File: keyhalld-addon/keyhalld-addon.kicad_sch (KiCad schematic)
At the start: 66 parts, among them J1 Conn_01x06_Pin, J2 USB_C_Receptacle_USB2.0_16P, J3 Conn_01x04_Pin, SW1 SW_Push, SW10 RST, SW2 SW_Push, SW3 SW_Push, SW4 SW_Push, SW5 SW_Push, SW6 SW_Push, SW7 SW_Push, SW8 SW_Push, SW9 BOOT, U1 TLV1117-33, U2 RP2350A, U3 USBLC6-2SC6, U4 ER_OLEDM0.91_1x-I2C, Y1 12MHz

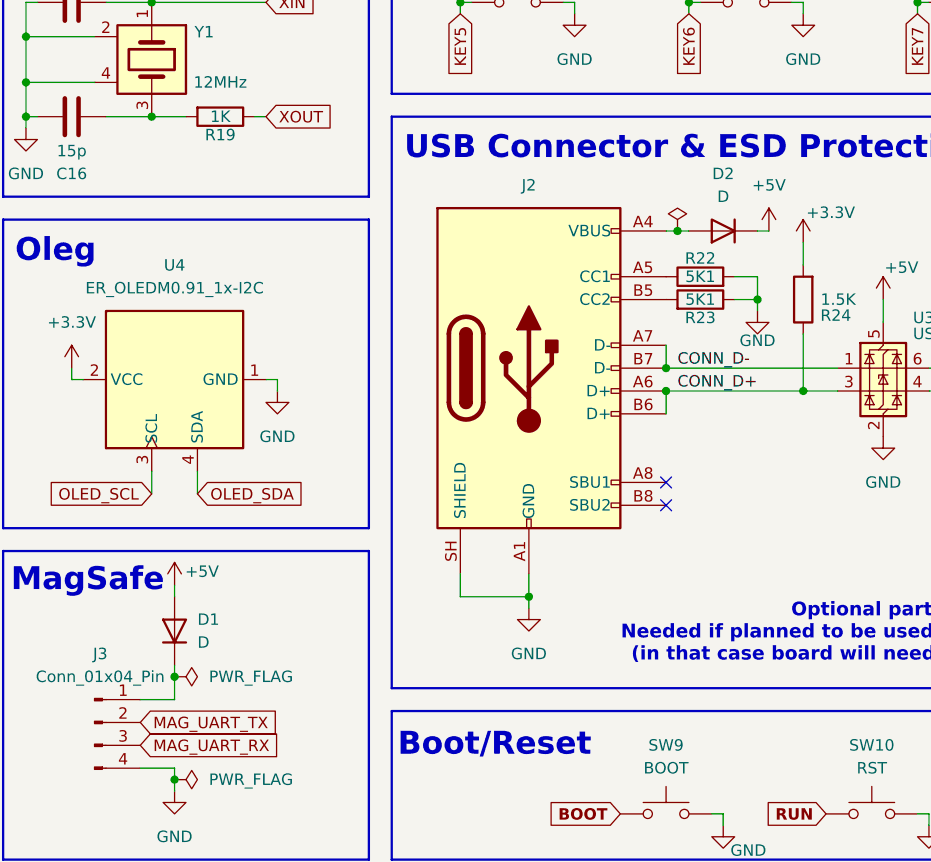
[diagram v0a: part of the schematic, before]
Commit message: fix diodes
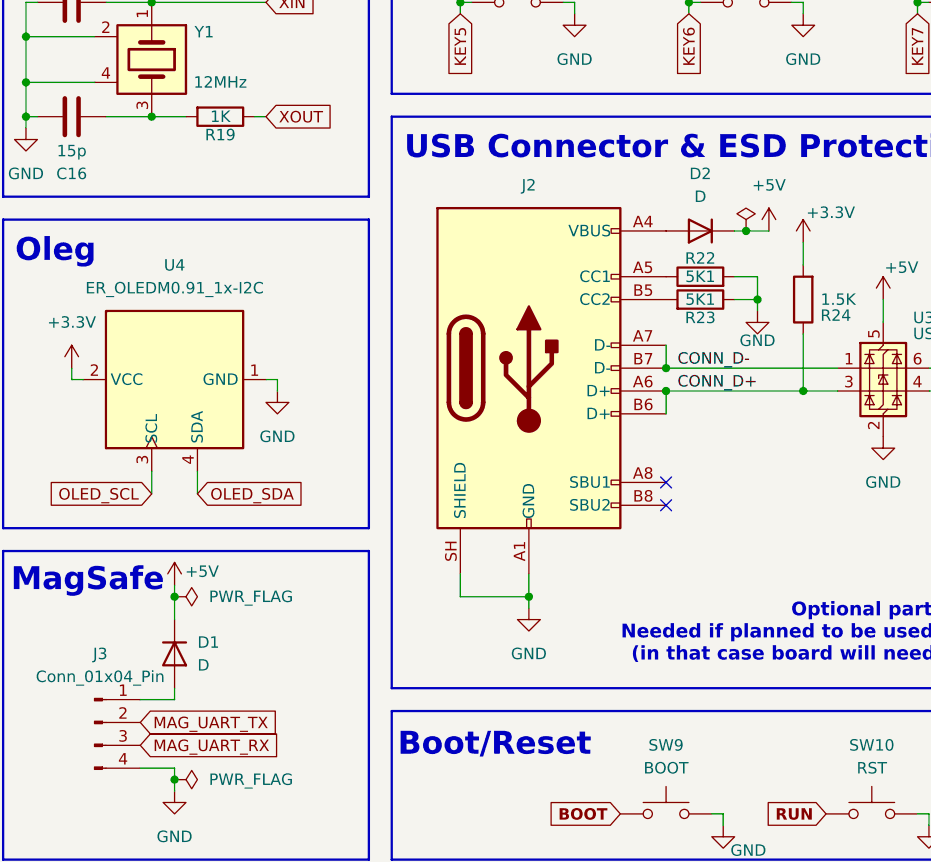
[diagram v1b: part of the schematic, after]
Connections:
- net +5V: now also D1.1 (K); no longer D1.2 (A)
- net at J3.1 (Pin_1): now also D1.2 (A); no longer D1.1 (K)

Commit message: add ws leds
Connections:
- net WS_LED: now reaches U2.41 (GPIO27_ADC1)
- no-connect marks 16 -> 15
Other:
- added sheet ws leds (ws_leds.kicad_sch)
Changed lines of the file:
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@@
 	)
 	(no_connect
-		(at 252.73 111.76)
-	)
-	(no_connect
 		(at 207.01 87.63)
 	)
@@
 		)
 	)
+	(global_label "WS_LED"
+		(shape input)
+		(at 252.73 111.76 0)
+		(fields_autoplaced yes)
+		(effects
+			(font
+				(size 1.27 1.27)
+			)
+			(justify left)
+		)
+		(property "Intersheetrefs" "${INTERSHEET_REFS}"
+			(at 262.7908 111.76 0)
+			(hide yes)
+			(show_name no)
+			(do_not_autoplace no)
+			(effects
+				(font
+					(size 1.27 1.27)
+				)
+				(justify left)
+			)
+		)
+	)
 	(global_label "EN_S_A"
 		(shape input)
@@
 				)
 			)
+		)
+	)
+	(sheet
+		(at 138.43 140.97)
+		(size 35.56 35.56)
+		(exclude_from_sim no)
+		(in_bom yes)
+		(on_board yes)
+		(dnp no)
+		(fields_autoplaced yes)
+		(stroke
+			(width 0.1524)
+			(type solid)
+		)
+		(fill
+			(color 204 204 255 1)
+		)
+		(property "Sheetname" "ws leds"
+			(at 138.43 140.2584 0)
+			(show_name no)
+			(do_not_autoplace no)
+			(effects
+				(font
+					(size 1.27 1.27)
+				)
+				(justify left bottom)
+			)
+		)
+		(property "Sheetfile" "ws_leds.kicad_sch"
+			(at 138.43 177.1146 0)
+			(show_name no)
+			(do_not_autoplace no)
+			(effects
+				(font
+					(size 1.27 1.27)
+				)
+				(justify left top)
+			)
+		)
+		(instances
+			(project "keyhalld-addon"
+				(path "/a8efb6d5-6c80-4ac0-bb97-11d91837bb7f"
+					(page "2")
+				)
+			)

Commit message: Super changes; FInal!
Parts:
- J3: footprint Connector_Wire:SolderWire-0.127sqmm_1x04_P3.7mm_D0.48mm_OD1mm -> Connector_PinHeader_2.54mm:PinHeader_1x04_P2.54mm_Vertical
- renumbered D2 to D1, D1 to D2
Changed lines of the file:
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@@
 		(dnp no)
 		(fields_autoplaced yes)
-		(property "Reference" "D2"
+		(property "Reference" "D1"
 			(at 91.44 119.38 0)
 			(show_name no)
@@
 			(project "keyhalld-addon"
 				(path "/a8efb6d5-6c80-4ac0-bb97-11d91837bb7f"
-					(reference "D2")
+					(reference "D1")
 					(unit 1)
 				)
@@
 		(in_pos_files yes)
 		(dnp no)
-		(property "Reference" "#PWR058"
+		(property "Reference" "#PWR057"
 			(at 33.02 168.91 0)
 			(hide yes)
@@
 			(project "keyhalld-addon"
 				(path "/a8efb6d5-6c80-4ac0-bb97-11d91837bb7f"
-					(reference "#PWR058")
+					(reference "#PWR057")
 					(unit 1)
 				)
@@
 		(dnp no)
 		(fields_autoplaced yes)
-		(property "Reference" "#PWR057"
+		(property "Reference" "#PWR058"
 			(at 72.39 173.99 0)
 			(hide yes)
@@
 			(project "keyhalld-addon"
 				(path "/a8efb6d5-6c80-4ac0-bb97-11d91837bb7f"
-					(reference "#PWR057")
+					(reference "#PWR058")
 					(unit 1)
 				)
@@
 		(dnp no)
 		(fields_autoplaced yes)
-		(property "Reference" "D1"
+		(property "Reference" "D2"
 			(at 35.56 171.4499 90)
 			(show_name no)
@@
 			(project "keyhalld-addon"
 				(path "/a8efb6d5-6c80-4ac0-bb97-11d91837bb7f"
-					(reference "D1")
+					(reference "D2")
 					(unit 1)
 				)
@@
 			)
 		)
-		(property "Footprint" "Connector_Wire:SolderWire-0.127sqmm_1x04_P3.7mm_D0.48mm_OD1mm"
+		(property "Footprint" "Connector_PinHeader_2.54mm:PinHeader_1x04_P2.54mm_Vertical"
 			(at 24.13 180.34 0)
 			(hide yes)

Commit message: routed pcb for addon board
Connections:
- net USB_D-: now reaches R13.2, U2.51 (USB_DM)
- net USB_D+: now reaches R12.1, U2.52 (USB_DP)
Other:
- moved on the sheet: R12, R13
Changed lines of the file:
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@@
 	(wire
 		(pts
-			(xy 222.25 74.93) (xy 222.25 77.47)
+			(xy 222.25 64.77) (xy 222.25 72.39)
 		)
 		(stroke
@@
 	(wire
 		(pts
-			(xy 222.25 85.09) (xy 222.25 87.63)
+			(xy 222.25 80.01) (xy 222.25 87.63)
 		)
 		(stroke
@@
 	(wire
 		(pts
-			(xy 224.79 85.09) (xy 224.79 87.63)
+			(xy 224.79 80.01) (xy 224.79 87.63)
 		)
 		(stroke
@@
 	(wire
 		(pts
-			(xy 224.79 74.93) (xy 224.79 77.47)
+			(xy 224.79 64.77) (xy 224.79 72.39)
 		)
 		(stroke
@@
 		)
 	)
+	(label "USB_D-"
+		(at 224.79 87.63 90)
+		(effects
+			(font
+				(size 1.27 1.27)
+			)
+			(justify left bottom)
+		)
+	)
 	(label "CONN_D-"
 		(at 88.9 140.97 0)
@@
 		)
 	)
+	(label "USB_D+"
+		(at 222.25 87.63 90)
+		(effects
+			(font
+				(size 1.27 1.27)
+			)
+			(justify left bottom)
+		)
+	)
 	(label "CONN_D+"
 		(at 88.9 143.51 0)
@@
 		)
 	)
+	(label "D+"
+		(at 222.25 71.12 90)
+		(effects
+			(font
+				(size 1.27 1.27)
+			)
+			(justify left bottom)
+		)
+	)
+	(label "D-"
+		(at 224.79 71.12 90)
+		(effects
+			(font
+				(size 1.27 1.27)
+			)
+			(justify left bottom)
+		)
+	)
 	(global_label "WS_LED"
 		(shape input)
@@
 	(global_label "D+"
 		(shape input)
-		(at 222.25 74.93 90)
+		(at 222.25 64.77 90)
 		(fields_autoplaced yes)
 		(effects
@@
 		)
 		(property "Intersheetrefs" "${INTERSHEET_REFS}"
-			(at 222.25 69.1024 90)
+			(at 222.25 58.9424 90)
 			(hide yes)
 			(show_name no)
@@
 	(global_label "D-"
 		(shape input)
-		(at 224.79 74.93 90)
+		(at 224.79 64.77 90)
 		(fields_autoplaced yes)
 		(effects
@@
 		)
 		(property "Intersheetrefs" "${INTERSHEET_REFS}"
-			(at 224.79 69.1024 90)
+			(at 224.79 58.9424 90)
 			(hide yes)
 			(show_name no)
@@
 	(symbol
 		(lib_id "Device:R")
-		(at 224.79 81.28 0)
+		(at 224.79 76.2 0)
 		(mirror y)
 		(unit 1)
@@
 		(dnp no)
 		(property "Reference" "R13"
-			(at 226.822 81.28 90)
+			(at 226.822 76.2 90)
 			(show_name no)
 			(do_not_autoplace no)
@@
 		)
 		(property "Value" "22R"
-			(at 224.79 81.28 90)
+			(at 224.79 76.2 90)
 			(show_name no)
 			(do_not_autoplace no)
@@
 		)
 		(property "Footprint" "Resistor_SMD:R_0603_1608Metric_Pad0.98x0.95mm_HandSolder"
-			(at 226.568 81.28 90)
+			(at 226.568 76.2 90)
 			(hide yes)
 			(show_name no)
@@
 		)
 		(property "Datasheet" ""
-			(at 224.79 81.28 0)
+			(at 224.79 76.2 0)
 			(hide yes)
 			(show_name no)
@@
 		)
 		(property "Description" "Resistor"
-			(at 224.79 81.28 0)
+			(at 224.79 76.2 0)
 			(hide yes)
 			(show_name no)
@@
 	(symbol
 		(lib_id "Device:R")
-		(at 222.25 81.28 0)
+		(at 222.25 76.2 0)
 		(mirror x)
 		(unit 1)
@@
 		(dnp no)
 		(property "Reference" "R12"
-			(at 220.218 81.28 90)
+			(at 220.218 76.2 90)
 			(show_name no)
 			(do_not_autoplace no)
@@
 		)
 		(property "Value" "22R"
-			(at 222.25 81.28 90)
+			(at 222.25 76.2 90)
 			(show_name no)
 			(do_not_autoplace no)
@@
 		)
 		(property "Footprint" "Resistor_SMD:R_0603_1608Metric_Pad0.98x0.95mm_HandSolder"
-			(at 220.472 81.28 90)
+			(at 220.472 76.2 90)
 			(hide yes)
 			(show_name no)
@@
 		)
 		(property "Datasheet" ""
-			(at 222.25 81.28 0)
+			(at 222.25 76.2 0)
 			(hide yes)
 			(show_name no)
@@
 		)
 		(property "Description" "Resistor"
-			(at 222.25 81.28 0)
+			(at 222.25 76.2 0)
 			(hide yes)
 			(show_name no)

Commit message: stitching vias; one more hole
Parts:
- added H5: MountingHole_Pad, MountingHole:MountingHole_2.2mm_M2_DIN965_Pad, symbol Mechanical:MountingHole_Pad
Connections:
- net GND: now also H5.1
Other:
- moved on the sheet: H1, H2, H3, H4
